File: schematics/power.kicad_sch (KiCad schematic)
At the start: 0 parts

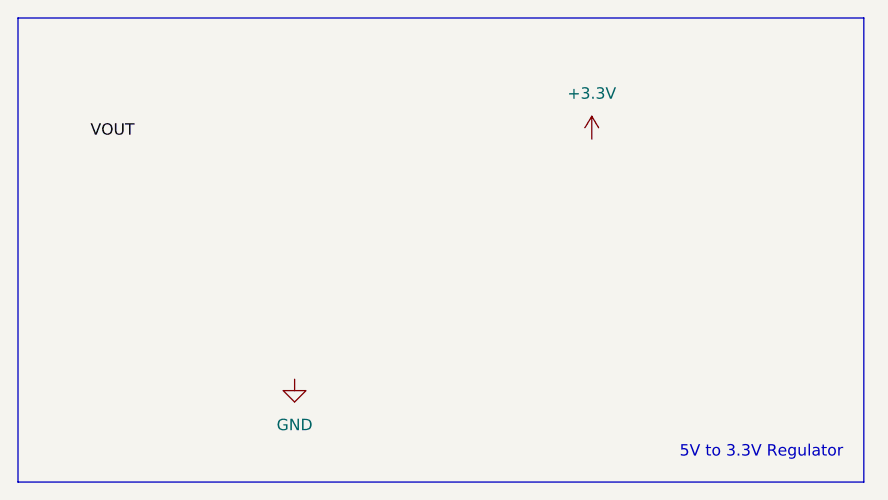
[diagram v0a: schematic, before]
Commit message: Update colors
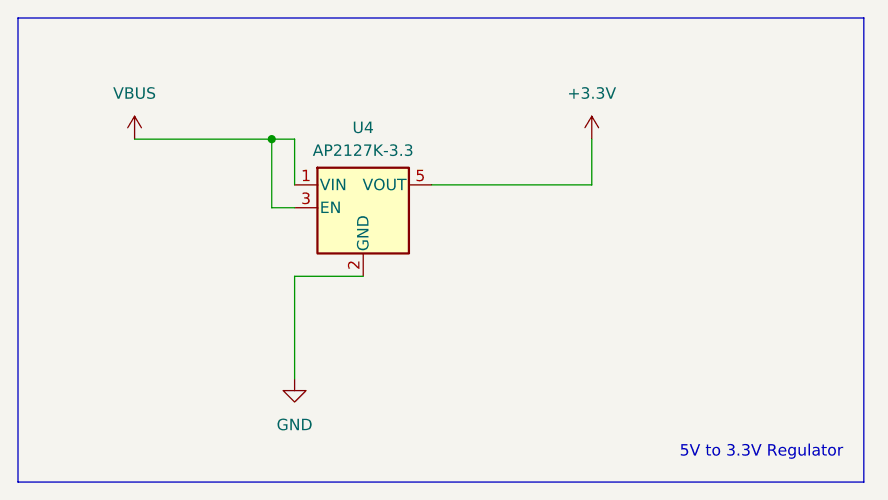
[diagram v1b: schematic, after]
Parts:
- added U4: AP2127K-3.3, Package_TO_SOT_SMD:SOT-23-5, symbol Regulator_Linear:AP2127K-3.3
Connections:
- net +3.3V: now also U4.5 (VOUT)
- net GND: now also U4.2 (GND)
- new net VBUS: U4.1 (VIN), U4.3 (EN)
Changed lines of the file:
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@@
 		)
 	)
-	(label "VOUT"
-		(at 33.02 33.02 180)
-		(effects
-			(font
-				(size 1.27 1.27)
-			)
-			(justify right bottom)
-		)
-	)
+	(junction
+		(at 48.26 33.02)
+		(diameter 0)
+		(color 0 0 0 0)
+	)
+	(wire
+		(pts
+			(xy 33.02 33.02) (xy 48.26 33.02)
+		)
+		(stroke
+			(width 0)
+			(type default)
+		)
+	)
+	(wire
+		(pts
+			(xy 83.82 38.1) (xy 83.82 33.02)
+		)
+		(stroke
+			(width 0)
+			(type default)
+		)
+	)
+	(wire
+		(pts
+			(xy 48.26 40.64) (xy 48.26 33.02)
+		)
+		(stroke
+			(width 0)
+			(type default)
+		)
+	)
+	(wire
+		(pts
+			(xy 48.26 33.02) (xy 50.8 33.02)
+		)
+		(stroke
+			(width 0)
+			(type default)
+		)
+	)
+	(wire
+		(pts
+			(xy 50.8 33.02) (xy 50.8 38.1)
+		)
+		(stroke
+			(width 0)
+			(type default)
+		)
+	)
+	(wire
+		(pts
+			(xy 58.42 48.26) (xy 50.8 48.26)
+		)
+		(stroke
+			(width 0)
+			(type default)
+		)
+	)
+	(wire
+		(pts
+			(xy 50.8 48.26) (xy 50.8 59.69)
+		)
+		(stroke
+			(width 0)
+			(type default)
+		)
+	)
+	(wire
+		(pts
+			(xy 66.04 38.1) (xy 83.82 38.1)
+		)
+		(stroke
+			(width 0)
+			(type default)
+		)
+	)
+	(wire
+		(pts
+			(xy 50.8 40.64) (xy 48.26 40.64)
+		)
+		(stroke
+			(width 0)
+			(type default)
+		)
+	)
+	(symbol
+		(lib_id "power:VBUS")
+		(at 33.02 33.02 0)
+		(unit 1)
+		(exclude_from_sim no)
+		(in_bom yes)
+		(on_board yes)
+		(dnp no)
+		(fields_autoplaced yes)
+		(property "Reference" "#PWR030"
+			(at 33.02 36.83 0)
+			(effects
+				(font
+					(size 1.27 1.27)
+				)
+				(hide yes)
+			)
+		)
+		(property "Value" "VBUS"
+			(at 33.02 27.94 0)
+			(effects
+				(font
+					(size 1.27 1.27)
+				)
+			)
+		)
+		(property "Footprint" ""
+			(at 33.02 33.02 0)
+			(effects
+				(font
+					(size 1.27 1.27)
+				)
+				(hide yes)
+			)
+		)
+		(property "Datasheet" ""
+			(at 33.02 33.02 0)
+			(effects
+				(font
+					(size 1.27 1.27)
+				)
+				(hide yes)
+			)
+		)
+		(property "Description" "Power symbol creates a global label with name \"VBUS\""
+			(at 33.02 33.02 0)
+			(effects
+				(font
+					(size 1.27 1.27)
+				)
+				(hide yes)
+			)
+		)
+		(pin "1"
+		)
+		(instances
+			(project ""
+				(path "/f2af4cd4-99cf-4d01-92f6-6413371e0fe3/8a3d119c-67dd-4f4a-8377-40fc3a7c71aa"
+					(reference "#PWR030")
+					(unit 1)
+				)
+			)
+		)
+	)
+	(symbol
+		(lib_id "Regulator_Linear:AP2127K-3.3")
+		(at 58.42 40.64 0)
+		(unit 1)
+		(exclude_from_sim no)
+		(in_bom yes)
+		(on_board yes)
+		(dnp no)
+		(fields_autoplaced yes)
+		(property "Reference" "U4"
+			(at 58.42 31.75 0)
+			(effects
+				(font
+					(size 1.27 1.27)
+				)
+			)
+		)
+		(property "Value" "AP2127K-3.3"
+			(at 58.42 34.29 0)
+			(effects
+				(font
+					(size 1.27 1.27)
+				)
+			)
+		)
+		(property "Footprint" "Package_TO_SOT_SMD:SOT-23-5"
+			(at 58.42 32.385 0)
+			(effects
+				(font
+					(size 1.27 1.27)
+				)
+				(hide yes)
+			)
+		)
+		(property "Datasheet" "https://www.diodes.com/assets/Datasheets/AP2127.pdf"
+			(at 58.42 38.1 0)
+			(effects
+				(font
+					(size 1.27 1.27)
+				)
+				(hide yes)
+			)
+		)
+		(property "Description" "300mA low dropout linear regulator, shutdown pin, 2.5V-6V input voltage, 3.3V fixed positive output, SOT-23-5"
+			(at 58.42 40.64 0)
+			(effects
+				(font
+					(size 1.27 1.27)
+				)
+				(hide yes)
+			)
+		)
+		(property "LCSC" "C156285"
+			(at 58.42 40.64 0)
+			(effects
+				(font
+					(size 1.27 1.27)
+				)
+				(hide yes)
+			)
+		)
+		(pin "1"
+		)
+		(pin "3"
+		)
+		(pin "2"
+		)
+		(pin "4"
+		)
+		(pin "5"
+		)
+		(instances
+			(project ""
+				(path "/f2af4cd4-99cf-4d01-92f6-6413371e0fe3/8a3d119c-67dd-4f4a-8377-40fc3a7c71aa"
+					(reference "U4")
+					(unit 1)
+				)
+			)
+		)
+	)

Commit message: Fix layout, rewiring, and clearances
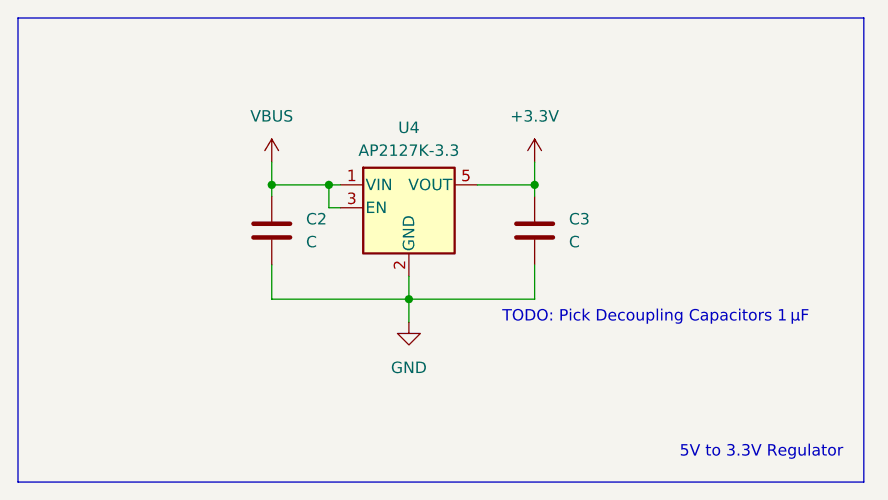
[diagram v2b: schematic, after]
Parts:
- added C2, C3: C, Capacitor_SMD:C_0201_0603Metric, symbol Device:C
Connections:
- net +3.3V: now also C3.1
- net GND: now also C2.2, C3.2
- net VBUS: now also C2.1
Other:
- note added: "TODO: Pick Decoupling Capacitors 1 µF"
- moved on the sheet: U4
